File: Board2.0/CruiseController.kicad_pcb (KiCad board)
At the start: 2 copper layers, 21.8 x 38 mm, 53 parts, among them J1 USB_B_Micro, J2 Conn_02x09_Top_Bottom, U1 ADG884, U3 TLV9064IRTER, U5 MIC5225, U6 MCP2562-E-MF, U7 STM32L433CCUx, Y1 32.768

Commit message: V2 replace LED
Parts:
- added R10: 27, Resistor_SMD:R_0603_1608Metric, B.Cu at (104.4, 89.9)
- added R21: 75, Resistor_SMD:R_0603_1608Metric, B.Cu at (104.4, 88.3)
- added R9: 27, Resistor_SMD:R_0603_1608Metric, B.Cu at (104.4, 91.5)
- D1: value IN-PI42TASPRPGPB -> 155124M173200-VeridianDesigns-CruiseController-rescue; footprint VeridianDesigns:IN-PI42TASPRPGPB -> VeridianDesigns:LED_155124M173200
- moved D1 2.20 mm to (101.5, 90.1), turned to 90 degrees
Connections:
- D1 pad 1: LEDDATA -> 3V3
- D1 pad 2: REGIN -> Net-(D1-Pad2)
- D1 pad 4: GND -> Net-(D1-Pad4)
- U7 pad 28: LEDDATA -> LEDB
- U7 pad 29: Net-(U7-Pad29) -> LEDG
- U7 pad 30: Net-(U7-Pad30) -> LEDR
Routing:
- net LEDDATA: track 15.5 -> 0.00 mm
- net LEDB: track 0.00 -> 12.0 mm
- net LEDG: track 0.00 -> 11.5 mm
- net LEDR: track 0.00 -> 10.6 mm
- net 3V3: track 105.4 -> 108.1 mm
- net Net-(D1-Pad4): track 0.00 -> 2.27 mm
- net Net-(D1-Pad2): track 0.00 -> 2.23 mm
- net Net-(D1-Pad3): track 0.00 -> 1.94 mm
- net REGIN: track 107.0 -> 106.6 mm, vias 5 -> 4
- net GND: vias 22 -> 20

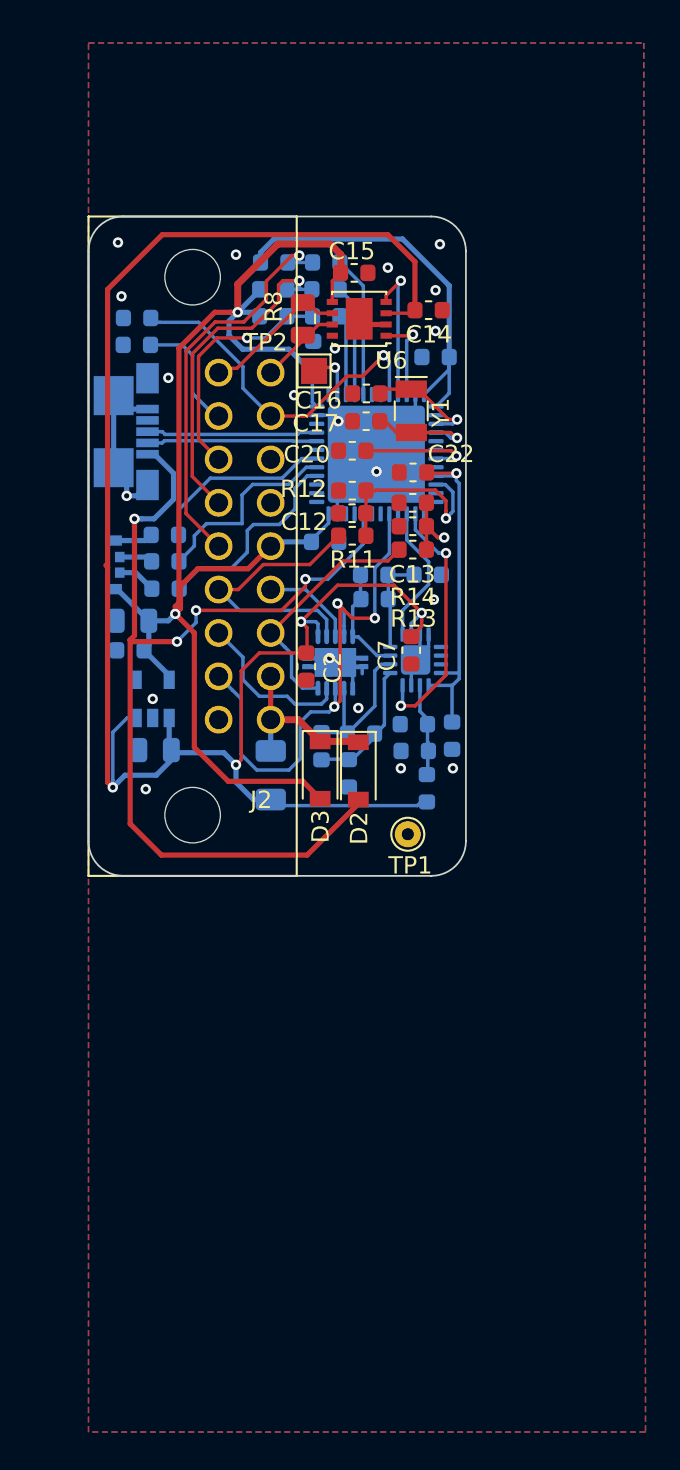
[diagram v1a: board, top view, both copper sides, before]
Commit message: Update V2
increase usb area
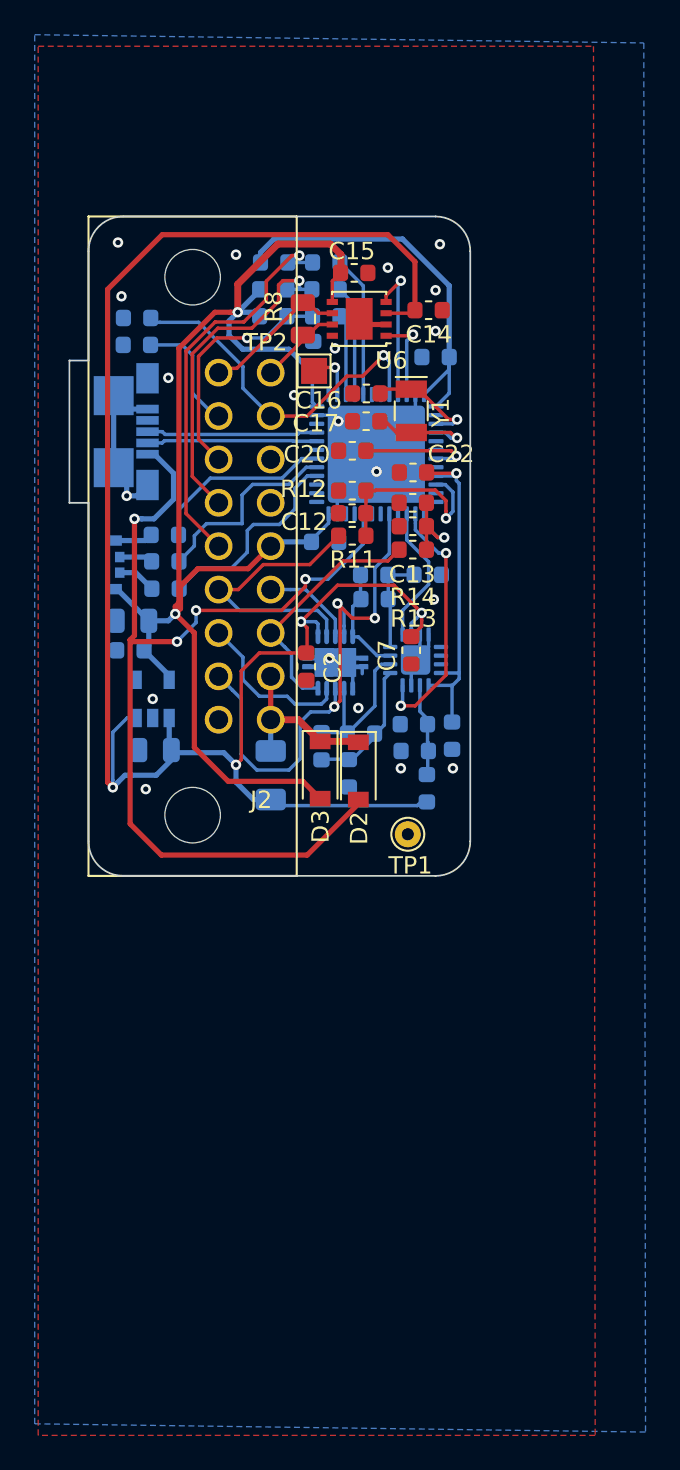
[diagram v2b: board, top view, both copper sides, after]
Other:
- board size 21.8 x 38 mm -> 23.1 x 38 mm
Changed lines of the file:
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@@
-(kicad_pcb (version 20171130) (host pcbnew "(5.1.4)-1")
+(kicad_pcb (version 20171130) (host pcbnew "(5.1.0)-1")
   (general
     (thickness 1.6)
-    (drawings 8)
-    (tracks 502)
+    (drawings 12)
+    (tracks 501)
     (zones 0)
     (modules 56)
@@
   (page A4)
   (layers
-    (0 F.Cu signal hide)
+    (0 F.Cu signal)
     (31 B.Cu signal)
     (32 B.Adhes user hide)
@@
     )
   )
+  (gr_line (start 100 86.5) (end 100 106) (layer Edge.Cuts) (width 0.1))
+  (gr_line (start 98.9 86.5) (end 100 86.5) (layer Edge.Cuts) (width 0.1))
+  (gr_line (start 98.9 78.3) (end 98.9 86.5) (layer Edge.Cuts) (width 0.1))
+  (gr_line (start 100 78.3) (end 98.9 78.3) (layer Edge.Cuts) (width 0.1))
+  (gr_line (start 100 72) (end 100 78.3) (layer Edge.Cuts) (width 0.1))
   (gr_arc (start 102 72) (end 102 70) (angle -90) (layer Edge.Cuts) (width 0.1))
-  (gr_arc (start 119.75 72) (end 121.75 72) (angle -90) (layer Edge.Cuts) (width 0.1))
-  (gr_arc (start 119.75 106) (end 119.75 108) (angle -90) (layer Edge.Cuts) (width 0.1))
+  (gr_arc (start 120 72) (end 122 72) (angle -90) (layer Edge.Cuts) (width 0.1))
+  (gr_arc (start 120 106) (end 120 108) (angle -90) (layer Edge.Cuts) (width 0.1))
   (gr_arc (start 102 106) (end 100 106) (angle -90) (layer Edge.Cuts) (width 0.1))
-  (gr_line (start 100 72) (end 100 106) (layer Edge.Cuts) (width 0.1))
-  (gr_line (start 119.75 108) (end 102 108) (layer Edge.Cuts) (width 0.1))
-  (gr_line (start 121.75 72) (end 121.75 106) (layer Edge.Cuts) (width 0.1))
-  (gr_line (start 102 70) (end 119.75 70) (layer Edge.Cuts) (width 0.1))
+  (gr_line (start 120 108) (end 102 108) (layer Edge.Cuts) (width 0.1))
+  (gr_line (start 122 72) (end 122 106) (layer Edge.Cuts) (width 0.1))
+  (gr_line (start 102 70) (end 120 70) (layer Edge.Cuts) (width 0.1))
   (via (at 116.6 84.7) (size 0.6) (drill 0.3) (layers F.Cu B.Cu) (net 1))
   (segment (start 117.3375 84.45) (end 116.5875 83.7) (width 0.2) (layer B.Cu) (net 1))
@@
   (segment (start 118.8125 75.4) (end 118.8125 72.607502) (width 0.3) (layer F.Cu) (net 30))
   (segment (start 118.8125 72.607502) (end 117.254998 71.05) (width 0.3) (layer F.Cu) (net 30))
-  (segment (start 101.100001 90.200001) (end 101.000011 90.100011) (width 0.3) (layer F.Cu) (net 30))
   (segment (start 101.4 102.475736) (end 101.4 102.9) (width 0.2) (layer B.Cu) (net 30))
   (segment (start 101.4 99.725) (end 101.4 102.475736) (width 0.2) (layer B.Cu) (net 30))
@@
     (polygon
       (pts
-        (xy 132.1 140.05) (xy 100 140.05) (xy 100 60) (xy 132 60)
+        (xy 129.2 140.240683) (xy 97.1 140.240683) (xy 97.1 60.190683) (xy 129.1 60.190683)
       )
     )
@@
     (polygon
       (pts
-        (xy 132.1 140.05) (xy 100 140.05) (xy 100 60) (xy 132 60)
+        (xy 132.1 140.05) (xy 96.9 139.575) (xy 96.9 59.525) (xy 132 60)
       )
     )

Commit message: udpate v2 pcb
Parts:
- added R22: 75, Resistor_SMD:R_0603_1608Metric, F.Cu at (119.8, 101.1)
- added R23: 75, Resistor_SMD:R_0603_1608Metric, F.Cu at (120.4, 104.1)
- added U2: CPC1017N, Package_SO:SOP-4_3.8x4.1mm_P2.54mm, B.Cu at (112.7, 104.5)
- F1: moved to F.Cu
- moved F1 7.31 mm to (117.8, 101.8)
- moved C13 3.10 mm to (118.7, 89.6)
- moved R13 1.70 mm to (118.7, 90.9)
- moved C2 1.12 mm to (113.3, 95.1), turned to 180 degrees
- moved R3 1.11 mm to (115.8, 101.3), turned to 180 degrees
- moved R14 0.85 mm to (118.7, 87.0)
- moved C7 0.80 mm to (117.8, 95.0)
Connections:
- J1 pad 4: Net-(J1-Pad4) -> (no net)
- J2 pad 1: VIN -> HZ1
- J2 pad 10: GND -> HZ0
- J2 pad 11: INTERSW -> GND
- U3 pad 5: Net-(U3-Pad5) -> (no net)
- U5 pad 4: Net-(U5-Pad4) -> (no net)
- U7 pad 11: Net-(U7-Pad11) -> (no net)
- U7 pad 12: Net-(U7-Pad12) -> (no net)
- U7 pad 16: Net-(U7-Pad16) -> HZEN
- U7 pad 18: Net-(U7-Pad18) -> (no net)
- U7 pad 19: Net-(U7-Pad19) -> (no net)
- U7 pad 2: Net-(U7-Pad2) -> (no net)
- U7 pad 21: Net-(U7-Pad21) -> (no net)
- U7 pad 22: Net-(U7-Pad22) -> (no net)
- U7 pad 25: Net-(U7-Pad25) -> (no net)
- U7 pad 26: Net-(U7-Pad26) -> (no net)
- U7 pad 27: Net-(U7-Pad27) -> (no net)
- U7 pad 31: Net-(U7-Pad31) -> (no net)
- U7 pad 34: Net-(U7-Pad34) -> (no net)
- U7 pad 37: Net-(U7-Pad37) -> (no net)
- U7 pad 42: Net-(U7-Pad42) -> (no net)
- U7 pad 43: Net-(U7-Pad43) -> (no net)
- U7 pad 5: Net-(U7-Pad5) -> (no net)
- U7 pad 6: Net-(U7-Pad6) -> (no net)
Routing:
- net HZEN: track 0.00 -> 17.3 mm, vias 0 -> 1
- net INTERSW: track 31.7 -> 18.9 mm
- net Net-(R23-Pad1): track 0.00 -> 9.48 mm, vias 0 -> 1
- net REGIN: track 106.5 -> 115.5 mm, vias 4 -> 5
- net HZ0: track 0.00 -> 7.79 mm
- net HZ1: track 0.00 -> 4.45 mm
- net Net-(R22-Pad1): track 0.00 -> 1.66 mm
- net VREFB: track 6.06 -> 6.96 mm
- net TTBIN: track 14.2 -> 13.5 mm
- net GND: vias 20 -> 22

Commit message: update pcbv2
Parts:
- added C11: 4.7uF, Capacitor_SMD:C_0805_2012Metric, B.Cu at (101.7, 76.0)
- D1: value 155124M173200-VeridianDesigns-CruiseController-rescue -> QLS6B-FKW; footprint VeridianDesigns:LED_155124M173200 -> LED_SMD:LED_Cree-PLCC6_4.7x1.5mm
- R21, R22, R23: value 75 -> 85
- moved R26 3.82 mm to (105.2, 80.4), turned to 90 degrees
- moved R1 2.27 mm to (104.7, 77.1)
- moved R21 1.55 mm to (104.4, 89.9)
- moved R10 1.53 mm to (104.3, 88.3)
- moved J1 0.55 mm to (102.8, 82.4)
- moved D1 0.51 mm to (101.0, 89.8)
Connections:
- D1 pad 1: 3V3 -> Net-(D1-Pad1)
- D1 pad 2: Net-(D1-Pad2) -> GND
- D1 pad 4: Net-(D1-Pad4) -> GND
- J1 pad 4: (no net) -> Net-(J1-Pad4)
- R10 pad 2: Net-(D1-Pad3) -> Net-(D1-Pad5)
- R21 pad 2: Net-(D1-Pad4) -> Net-(D1-Pad3)
- R9 pad 2: Net-(D1-Pad2) -> Net-(D1-Pad1)
- U3 pad 5: (no net) -> Net-(U3-Pad5)
- U5 pad 4: (no net) -> Net-(U5-Pad4)
- U7 pad 11: (no net) -> Net-(U7-Pad11)
- U7 pad 12: (no net) -> Net-(U7-Pad12)
- U7 pad 18: (no net) -> Net-(U7-Pad18)
- U7 pad 19: (no net) -> Net-(U7-Pad19)
- U7 pad 2: (no net) -> Net-(U7-Pad2)
- U7 pad 21: (no net) -> Net-(U7-Pad21)
- U7 pad 22: (no net) -> Net-(U7-Pad22)
- U7 pad 25: (no net) -> Net-(U7-Pad25)
- U7 pad 26: (no net) -> Net-(U7-Pad26)
- U7 pad 27: (no net) -> Net-(U7-Pad27)
- U7 pad 29: LEDG -> LEDR
- U7 pad 30: LEDR -> LEDG
- U7 pad 31: (no net) -> Net-(U7-Pad31)
- U7 pad 34: (no net) -> Net-(U7-Pad34)
- U7 pad 37: (no net) -> Net-(U7-Pad37)
- U7 pad 42: (no net) -> Net-(U7-Pad42)
- U7 pad 43: (no net) -> Net-(U7-Pad43)
- U7 pad 5: (no net) -> Net-(U7-Pad5)
- U7 pad 6: (no net) -> Net-(U7-Pad6)
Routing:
- net 3V3: track 108.1 -> 112.8 mm
- net Net-(J2-Pad17): track 6.91 -> 2.48 mm
- net Net-(D1-Pad1): track 0.00 -> 3.09 mm
- net Net-(D1-Pad5): track 0.00 -> 2.36 mm
- net Net-(D1-Pad4): track 2.27 -> 0.00 mm
- net Net-(D1-Pad2): track 2.23 -> 0.00 mm
- net BOOT0: track 20.2 -> 18.2 mm
- net GND: track 40.9 -> 39.7 mm, vias 22 -> 24
- net LEDG: track 11.5 -> 10.6 mm
- net Net-(D1-Pad3): track 1.94 -> 2.49 mm
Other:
- board size 23.1 x 38 mm -> 23.8 x 38 mm

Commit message: update pcb v2
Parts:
- removed R22, R23: 85, Resistor_SMD:R_0603_1608Metric
- removed U2: CPC1017N, Package_SO:SOP-4_3.8x4.1mm_P2.54mm
- R21: value 85 -> 84.5
- moved TP1 1.03 mm to (117.8, 106.4)
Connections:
- J2 pad 1: HZ1 -> VIN
- J2 pad 10: HZ0 -> GND
- U3 pad 4: GND -> Net-(U3-Pad4)
- U3 pad 5: Net-(U3-Pad5) -> Net-(U3-Pad4)
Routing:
- net Net-(R23-Pad1): track 9.48 -> 0.00 mm, vias 1 -> 0
- net HZ0: track 7.79 -> 0.00 mm
- net HZ1: track 4.45 -> 0.00 mm
- net Net-(U3-Pad4): track 0.00 -> 1.19 mm
- net VIN: track 9.44 -> 10.4 mm
- net GND: track 39.7 -> 40.4 mm, vias 24 -> 25
